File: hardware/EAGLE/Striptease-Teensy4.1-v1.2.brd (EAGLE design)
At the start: 83.8 x 40.6 mm, 11 parts

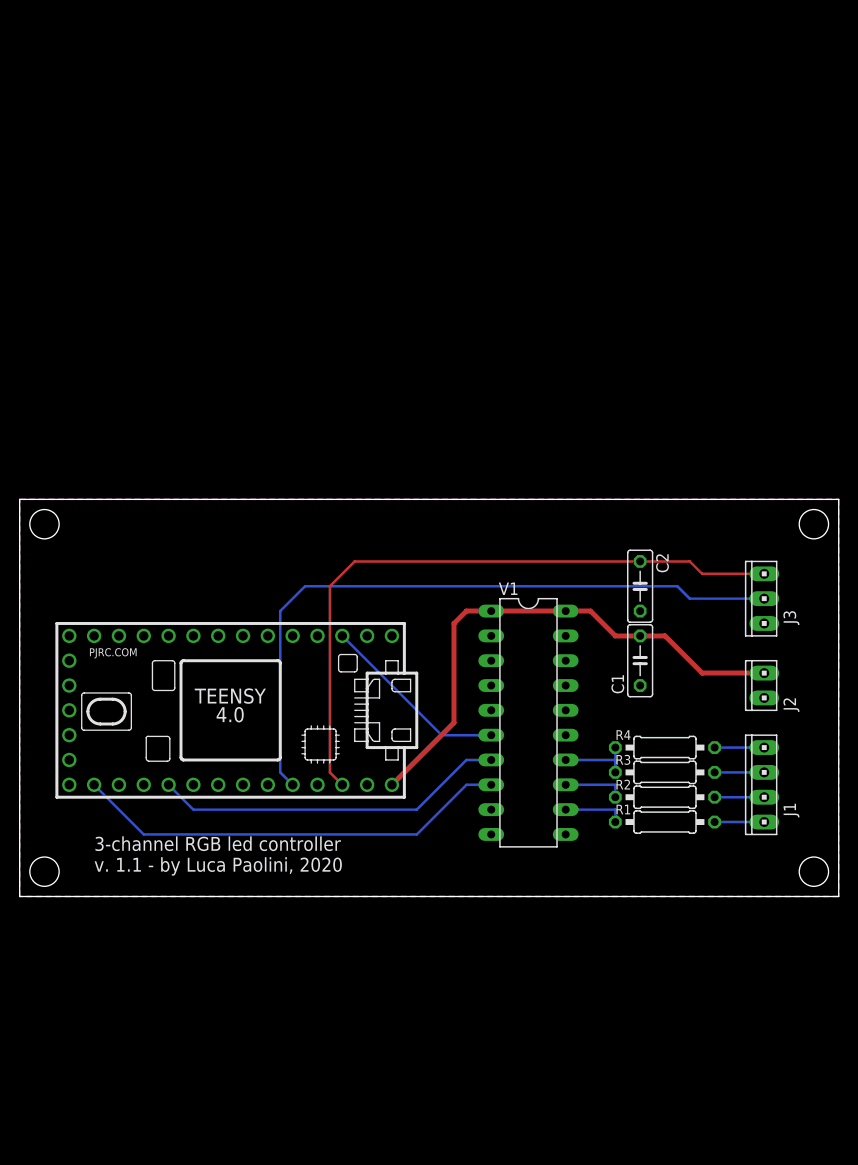
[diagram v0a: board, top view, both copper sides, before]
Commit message: Change connector names in EAGLE boards.
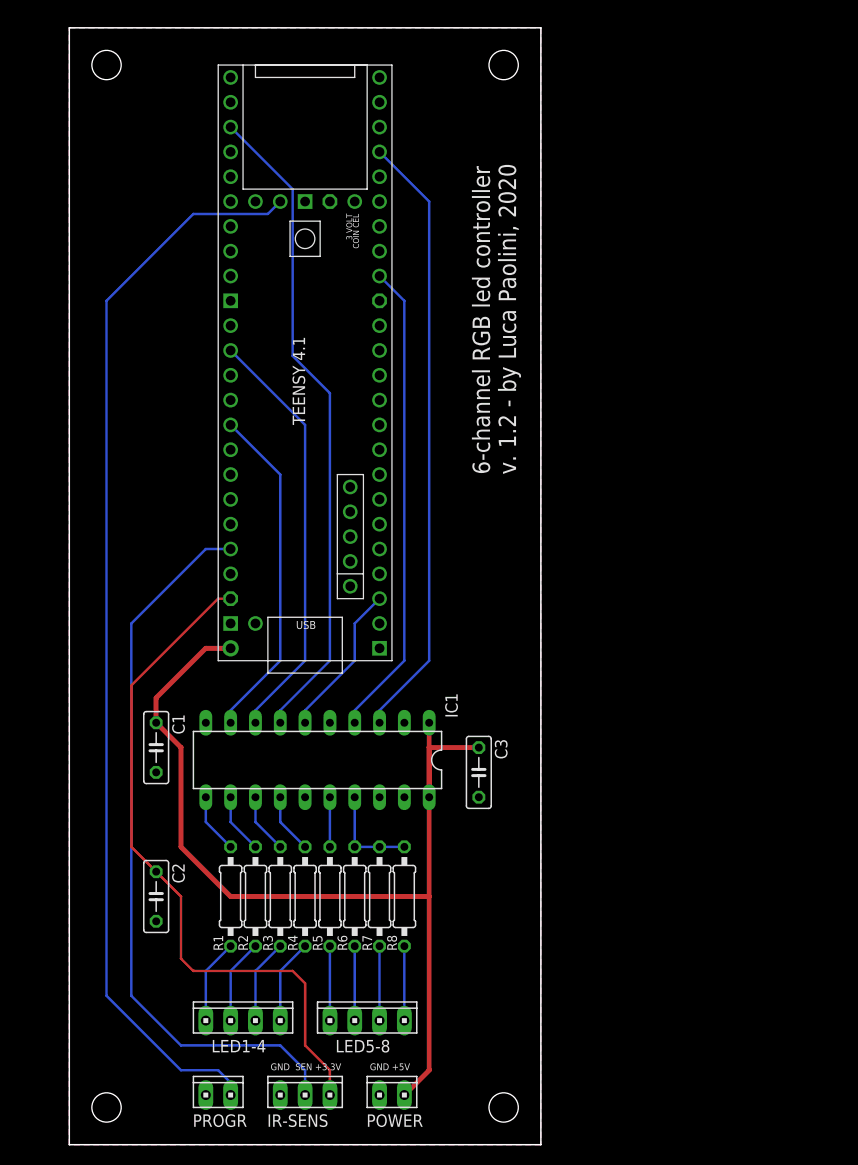
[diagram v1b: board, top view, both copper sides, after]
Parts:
- removed J1: (no value), con-amp:10X04MTA
- removed J2: (no value), con-amp:10X02MTA
- removed J3: (no value), con-amp:10X03MTA
- removed U$1: TEENSY_4.0-BASIC, Teensy-4.0:TEENSY_4.0-BASIC
- removed V1: 74245N, 74ttl-din:DIL20
- added C3: 100n, rcl:C050-025X075
- added IC1: 74245N, 74ttl-din:DIL20
- added IR-SENS: (no value), con-amp:10X03MTA
- added LED1-4, LED5-8: (no value), con-amp:10X04MTA
- added POWER, PROGR: (no value), con-amp:10X02MTA
- added R5, R6, R7, R8: 100, rcl:0207/10
- added U$3: TEENSY41-E, teensy:TENNSY41-E
- moved C2 58.8 mm to (12.7, 21.6)
- moved C1 50.3 mm to (12.7, 36.8), turned to 270 degrees
- moved R1 45.1 mm to (20.3, 21.6), turned to 270 degrees
- moved R2 43.1 mm to (22.9, 21.6), turned to 270 degrees
- moved R3 41.4 mm to (25.4, 21.6), turned to 270 degrees
- moved R4 39.9 mm to (27.9, 21.6), turned to 270 degrees
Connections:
- removed net N$21: U$1.1/TX, V1.6
- removed net N$5: J1.1, R4.2
- new net N$16: IC1.14, R4.1
- new net N$19: LED1-4.1, R4.2
- new net N$20: LED5-8.4, R5.2
- new net N$22: LED5-8.3, R6.2
- new net N$23: IC1.9, U$3.17-A3/TX4/SDA1
- new net N$24: IC1.8, U$3.14-A0/TX3/SPDIF_OUT
- new net N$25: IC1.7, U$3.35-TX8
- new net N$26: IC1.6, U$3.1-TX1/MISO1/CTX2
- new net N$27: IC1.4, U$3.24-A10/TX6/SCL2
- new net N$28: IC1.3, U$3.29-TX7
- new net N$3: IC1.16, R5.1
- new net N$31: IR-SENS.2, U$3.22-A8/CTX1
- new net N$6: LED5-8.2, R7.2
- net +5V: now also C1.1, C3.1, IC1.1, IC1.20, POWER.1, U$3.VIN; no longer C1.2, J2.1, U$1.VIN, V1.1, V1.20
- net GND: now also C1.2, C3.2, IC1.10, IC1.19, IC1.2, IC1.5, IR-SENS.3, POWER.2, PROGR.2, U$3.GND1, U$3.GND2, U$3.GND3, U$3.GND6; no longer C1.1, J2.2, J3.3, U$1.GND, U$1.GND2, V1.10, V1.19, V1.2, V1.3, V1.4, V1.5, V1.9
- net N$1: now also C2.1, IR-SENS.1, U$3.3V3-3; no longer J3.2, U$1.22/A8
- net N$10: now also LED5-8.1, R8.2; no longer U$1.14/A0, V1.8
- net N$11: now also IC1.11; no longer V1.12
- net N$12: now also IC1.12; no longer V1.13
- net N$13: now also IC1.13; no longer R4.1, V1.14
- net N$14: now also IC1.17, R6.1, R7.1, R8.1; no longer U$1.17/A3, V1.7
- net N$2: now also PROGR.1, U$3.PROGRAM; no longer C2.1, J3.1, U$1.3V3_LO
- net N$7: now also LED1-4.2; no longer J1.2
- net N$8: now also LED1-4.3; no longer J1.3
- net N$9: now also LED1-4.4; no longer J1.4
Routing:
- net N$31: track 0.00 -> 74.9 mm
- net N$25: track 0.00 -> 67.3 mm
- net N$28: track 0.00 -> 62.6 mm
- net N$27: track 0.00 -> 48.9 mm
- net +5V: track 55.3 -> 102.8 mm
- net N$2: track 66.9 -> 110.8 mm
- net N$24: track 0.00 -> 43.4 mm
- net N$10: track 44.8 -> 7.62 mm
- net N$23: track 0.00 -> 34.7 mm
- net N$14: track 36.2 -> 10.2 mm
- net N$21: track 20.7 -> 0.00 mm
- net N$26: track 0.00 -> 15.9 mm
- net N$19: track 0.00 -> 8.67 mm
- net N$6: track 0.00 -> 7.62 mm
- net N$22: track 0.00 -> 7.62 mm
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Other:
- board size 83.8 x 40.6 mm -> 48.3 x 114.3 mm
- board text added: "6-channel RGB led controller v. 1.2 - by Luca Paolini, 2020"
- board text added: "GND +5V"
- board text added: "GND SEN +3.3V"
- board text removed: "3-channel RGB led controller v. 1.1 - by Luca Paolini, 2020"

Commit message: Add connector pinout for LEDs in EAGLE boards.
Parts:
- renumbered IR-SENS to IR-RECV
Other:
- board text added: "1 2 3 4"
- board text added: "5 6 6 6"
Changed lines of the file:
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@@
 <text x="34.29" y="3.81" size="0.7" layer="25" font="vector"> GND +5V</text>
 <text x="24.13" y="3.81" size="0.7" layer="25" font="vector"> GND  SEN +3.3V</text>
+<text x="16.51" y="11.43" size="0.9" layer="25" font="vector">  1    2    3    4</text>
+<text x="29.21" y="11.43" size="0.9" layer="25" font="vector">  5    6    6    6</text>
 </plain>
 <attributes>
@@
 <attribute name="VALUE" x="42.926" y="37.719" size="1.27" layer="27" ratio="10" rot="R270"/>
 </element>
-<element name="IR-SENS" library="con-amp" library_urn="urn:adsk.eagle:library:127" package="10X03MTA" package3d_urn="urn:adsk.eagle:package:8081621/1" value="" x="27.94" y="1.27" smashed="yes">
+<element name="IR-RECV" library="con-amp" library_urn="urn:adsk.eagle:library:127" package="10X03MTA" package3d_urn="urn:adsk.eagle:package:8081621/1" value="" x="27.94" y="1.27" smashed="yes">
 <attribute name="NAME" x="24.0538" y="-1.9812" size="1.27" layer="25" font="vector"/>
 <attribute name="POPULARITY" value="2" x="27.94" y="1.27" size="1.778" layer="27" display="off"/>
@@
 <wire x1="25.4" y1="6.35" x2="15.24" y2="6.35" width="0.254" layer="16"/>
 <wire x1="15.24" y1="6.35" x2="10.16" y2="11.43" width="0.254" layer="16"/>
-<contactref element="IR-SENS" pad="2"/>
+<contactref element="IR-RECV" pad="2"/>
 <wire x1="27.94" y1="3.81" x2="27.94" y2="1.27" width="0.254" layer="16"/>
 </signal>
@@
 <wire x1="27.94" y1="12.7" x2="26.67" y2="13.97" width="0.254" layer="1"/>
 <wire x1="26.67" y1="13.97" x2="16.51" y2="13.97" width="0.254" layer="1"/>
-<contactref element="IR-SENS" pad="1"/>
+<contactref element="IR-RECV" pad="1"/>
 <wire x1="30.48" y1="1.27" x2="30.48" y2="3.81" width="0.254" layer="1"/>
 <wire x1="30.48" y1="3.81" x2="27.94" y2="6.35" width="0.254" layer="1"/>
@@
 <contactref element="IC1" pad="10"/>
 <contactref element="POWER" pad="2"/>
-<contactref element="IR-SENS" pad="3"/>
+<contactref element="IR-RECV" pad="3"/>
 <contactref element="PROGR" pad="2"/>
 <contactref element="C2" pad="2"/>
